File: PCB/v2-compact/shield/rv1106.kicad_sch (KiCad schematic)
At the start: 0 parts

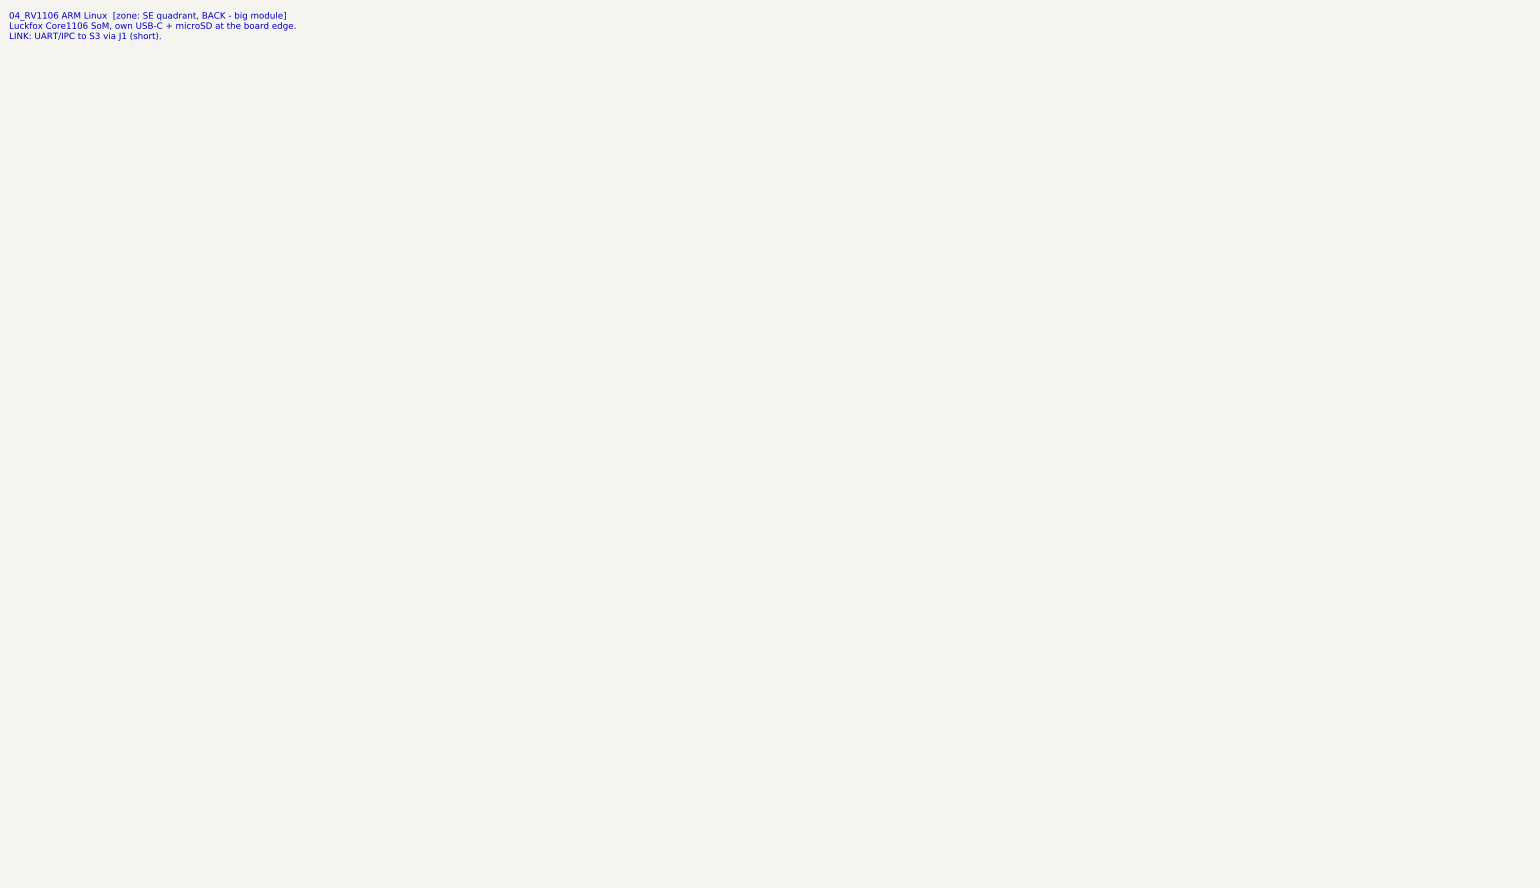
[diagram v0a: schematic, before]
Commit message: Schematics: HTRC110 and RV1106 sheets — full sheet set complete
- 08_LF_RFID_HTRC110: 5V HITAG reader, 3-wire (SCLK/DIN/DOUT) to the C5, DOUT
  open-drain pulled to 3.3V, 4MHz crystal, decoupling. LF coil tank flagged;
  pins 8-14 flagged to verify against the datasheet.
- 04_RV1106_Linux (A3): Core1106 SoM self-powered from its own USB-C (CC
  resistors) with its own microSD; UART to the S3 over J1 (RV_TX/RX/CTRL).
  Symbol is functional with placeholder pin numbers, flagged to verify against
  the Luckfox pinout.
- Add HTRC110 + RV1106 custom symbols to SnowOwl.kicad_sym.

All 17 sheets across both boards are now captured and netlist-verified
(153 nets). Remaining: ERC cleanup (no-connects + power flags), the two flagged
pinouts, RF matching values, and finishing the module footprints.
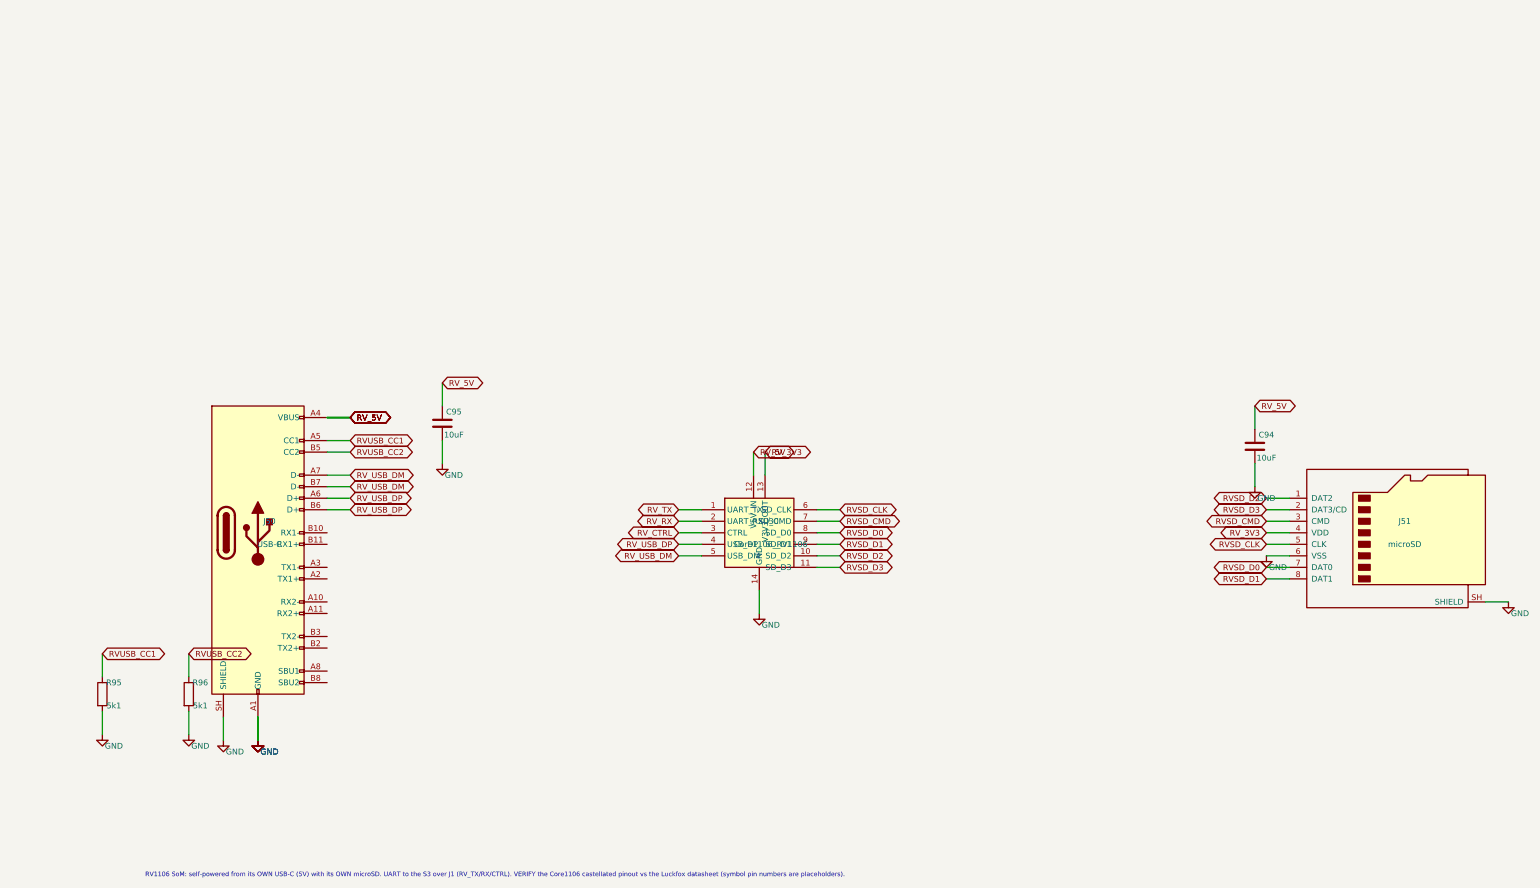
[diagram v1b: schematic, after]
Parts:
- added C94, C95: 10uF, Capacitor_SMD:C_0402_1005Metric, symbol Device:C
- added J50: USB-C, Connector_USB:USB_C_Receptacle_HRO_TYPE-C-31-M-12, symbol Connector:USB_C_Receptacle
- added J51: microSD, Connector_Card:microSD_HC_Hirose_DM3AT-SF-PEJM5, symbol Connector:Micro_SD_Card
- added R95, R96: 5k1, Resistor_SMD:R_0402_1005Metric, symbol Device:R
- added U30: Core1106_RV1106, symbol SnowOwl:RV1106_Core1106
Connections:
- new net GND: C94.2, C95.2, J50.A1 (GND), J50.A12 (GND), J50.B1 (GND), J50.B12 (GND), J50.SH (SHIELD), J51.6 (VSS), J51.SH (SHIELD), R95.2, R96.2, U30.14 (GND)
- new net RVSD_CLK: J51.5 (CLK), U30.6 (SD_CLK)
- new net RVSD_CMD: J51.3 (CMD), U30.7 (SD_CMD)
- new net RVSD_D0: J51.7 (DAT0), U30.8 (SD_D0)
- new net RVSD_D1: J51.8 (DAT1), U30.9 (SD_D1)
- new net RVSD_D2: J51.1 (DAT2), U30.10 (SD_D2)
- new net RVSD_D3: J51.2 (DAT3/CD), U30.11 (SD_D3)
- new net RVUSB_CC1: J50.A5 (CC1), R95.1
- new net RVUSB_CC2: J50.B5 (CC2), R96.1
- new net RV_3V3: J51.4 (VDD), U30.13 (V3V3_OUT)
- new net RV_5V: C94.1, C95.1, J50.A4 (VBUS), J50.A9 (VBUS), J50.B4 (VBUS), J50.B9 (VBUS), U30.12 (V5V_IN)
- new net RV_CTRL: U30.3 (CTRL)
- new net RV_RX: U30.2 (UART_RX)
- new net RV_TX: U30.1 (UART_TX)
- new net RV_USB_DM: J50.A7 (D-), J50.B7 (D-), U30.5 (USB_DM)
- new net RV_USB_DP: J50.A6 (D+), J50.B6 (D+), U30.4 (USB_DP)
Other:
- note added: "RV1106 SoM: self-powered from its OWN USB-C (5V) with its OWN microSD. UART to the S3 over J1 (RV_TX/RX/CTRL). VERIFY the Core1106 castellated pinout vs the Luckfox datasheet (symbol pin numbers are placeholders)."
- note removed: "04_RV1106 ARM Linux [zone: SE quadrant, BACK - big module] Luckfox Core1106 SoM, own USB-C + microSD at the board edge. LINK: UART/IPC to S3 via J1 (short)."

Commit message: Schematic: set U30 (RV1106) footprint (generator wrote it empty for the custom SnowOwl symbol)
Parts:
- U30: footprint (none) -> SnowOwl:RV1106_Core1106
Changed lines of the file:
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@@
     (property "Reference" "U30" (at 182.88 127 0) (effects (font (size 1.27 1.27))))
     (property "Value" "Core1106_RV1106" (at 182.88 132.08 0) (effects (font (size 1.27 1.27))))
-    (property "Footprint" "" (at 180.34 129.54 0) (effects (font (size 1.27 1.27)) hide))
+    (property "Footprint" "SnowOwl:RV1106_Core1106" (at 180.34 129.54 0) (effects (font (size 1.27 1.27)) hide))
     (pin "1")
     (pin "2")

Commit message: Schematic: add battery + USB-C charger power subsystem (BQ25896, 2500mAh)
Adds the full power section to the shield's power sheet, per the battery/stacking research:
- USB-C (J50 VBUS) -> BQ25896 (3A switch-mode charger + power-path + I2C). Charges a 2500mAh
  1S LiPo (BT50, JST-PH) through DW01A/FS8205 protection (U56); MAX17048 fuel gauge (U57).
- Power-path SYS -> TPS63020 buck-boost = system +3V3 (holds regulation as the cell sags),
  and -> TPS61230A boost = system +5V (feeds the RV1106). AP7361C LDO still makes clean C5_VDD.
- Rewired: J50 is now the charge/data input (VBUS), and the RV1106 is powered from the system
  +5V rail instead of being self-powered. +5V/+3V3 distribute to both boards over J1.
- New functional symbols (BQ25896/TPS63020/MAX17048/TPS61230A/DW01) in SnowOwl.kicad_sym.

Verified by KiCad's netlister: GND=79 (top net, intact), VBUS=3, VBAT=6, VSYS=8, +5V=13,
+3V3=36 - all rails distinct, no merges. Fixed two stub-collision shorts found while building
(input cap on the charger's pin column; VBAT power-flag on a cap column) and upgraded
find_shorts.py to catch pin-on-wire collisions, not just endpoint snaps.

FIRST-PASS: IC pinouts + passive values are placeholders to VERIFY vs datasheets. The power
PARTS still need placing on the PCB (next step), and the main board's own USB/LDO reconciled.
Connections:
- net RV_5V renamed VBUS
- net VBUS: no longer C94.1, C95.1, U30.12 (V5V_IN)
- new net +5V: C94.1, C95.1, U30.12 (V5V_IN)
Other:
- note added: "RV1106 SoM: powered from the system +5V rail (battery boost). J50 USB-C brings in VBUS (charge input) + its own USB data + microSD. UART to the S3 over J1 (RV_TX/RX/CTRL). VERIFY the Core1106 castellated pinout vs the Luckfox datasheet (symbol pin numbers are placeholders)."
- note removed: "RV1106 SoM: self-powered from its OWN USB-C (5V) with its OWN microSD. UART to the S3 over J1 (RV_TX/RX/CTRL). VERIFY the Core1106 castellated pinout vs the Luckfox datasheet (symbol pin numbers are placeholders)."

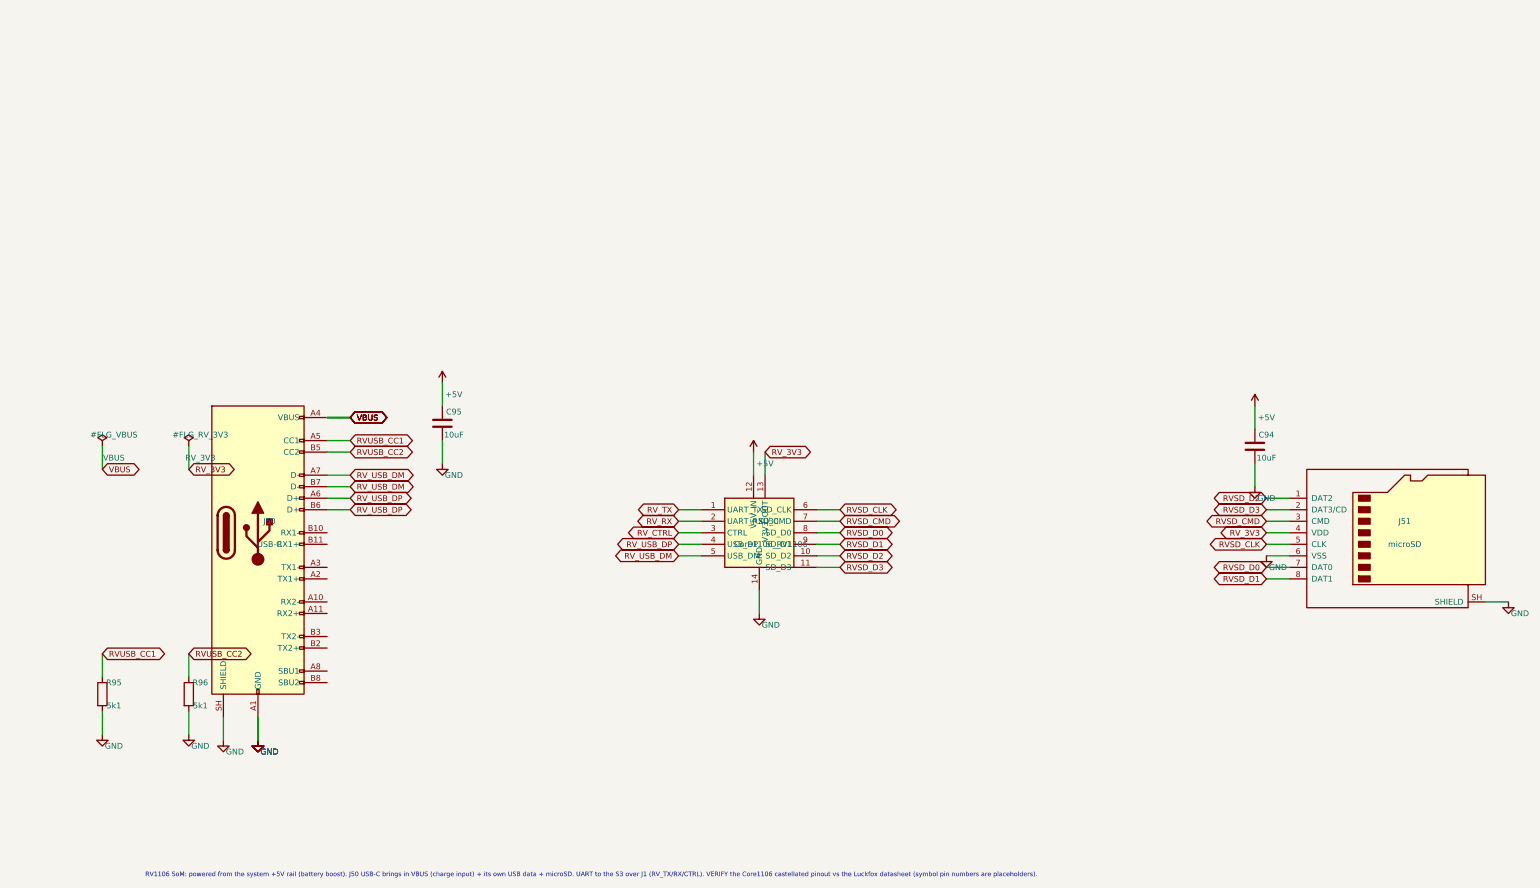
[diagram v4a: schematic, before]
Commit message: Single USB-C + battery power; J1 vertical on the left edge; U30 model; back-side comments
Power/architecture:
- Remove J50 (the RV1106's own USB-C). The device now has ONE USB-C: the main board's J20.
  J20's VBUS is carried over J1 pin19 (was SPARE) to the shield's BQ25896 charger, so charging +
  the ESP32-S3 data/programming share the single port. Everything runs off the battery.
- Reconcile the nets: J20 VBUS -> VBUS (was VBUS_MAIN), charger VBUS <- J1 pin19, RV1106 keeps its
  microSD (J51) but loses its USB port (reached over UART on J1). Removed orphans R95/R96 (J50 CC
  resistors) and the redundant main LDO U21. Verified: J1 mates 20/20 on both boards, VBUS spans
  J20 -> J1 -> U55, GND healthy (106/37 nodes), no bad net merges.

Placement:
- J1 stack header: was horizontal mid-board, now VERTICAL on the WEST edge at the same spot on both
  boards (they still mate). Nudged the shield's PN532/flash/HTRC (U7/U12/U8) east to clear it, and
  the main's screen east. Status LEDs D10/D11 pulled off the corner mounting holes. 0 real overlaps.

3D + silk:
- U30 (RV1106 Core1106): no KiCad model exists for the Luckfox SoM -> add a sized VRML module
  stand-in (SnowOwl.3dshapes/RV1106_Core1106.wrl; sizes pre-divided by 2.54 for KiCad's inch-unit
  VRML reader). USB-C model: swap the vertical USB4085 for the 16-pin horizontal USB4105 so it
  seats correctly against the horizontal HRO footprint.
- ESP32-BlackRaven art: logo moved to the top by the LEDs, raven dropped down to fill the board.
  Dropped the cluttering TFT label (fab outline kept). Added five back-side silkscreen comments on
  the main board (title/rev, battery, power path, USB-C role, J1 purpose).

Deferred (SWIG pcbnew geometry calls are failing in this environment right now): re-pour the inner
GND/+3V3 planes (inner layers, not visible in renders); apply the datasheet pinout/value fixes to
the power ICs (BQ25896/TPS63020/TPS61230A/MAX17048).
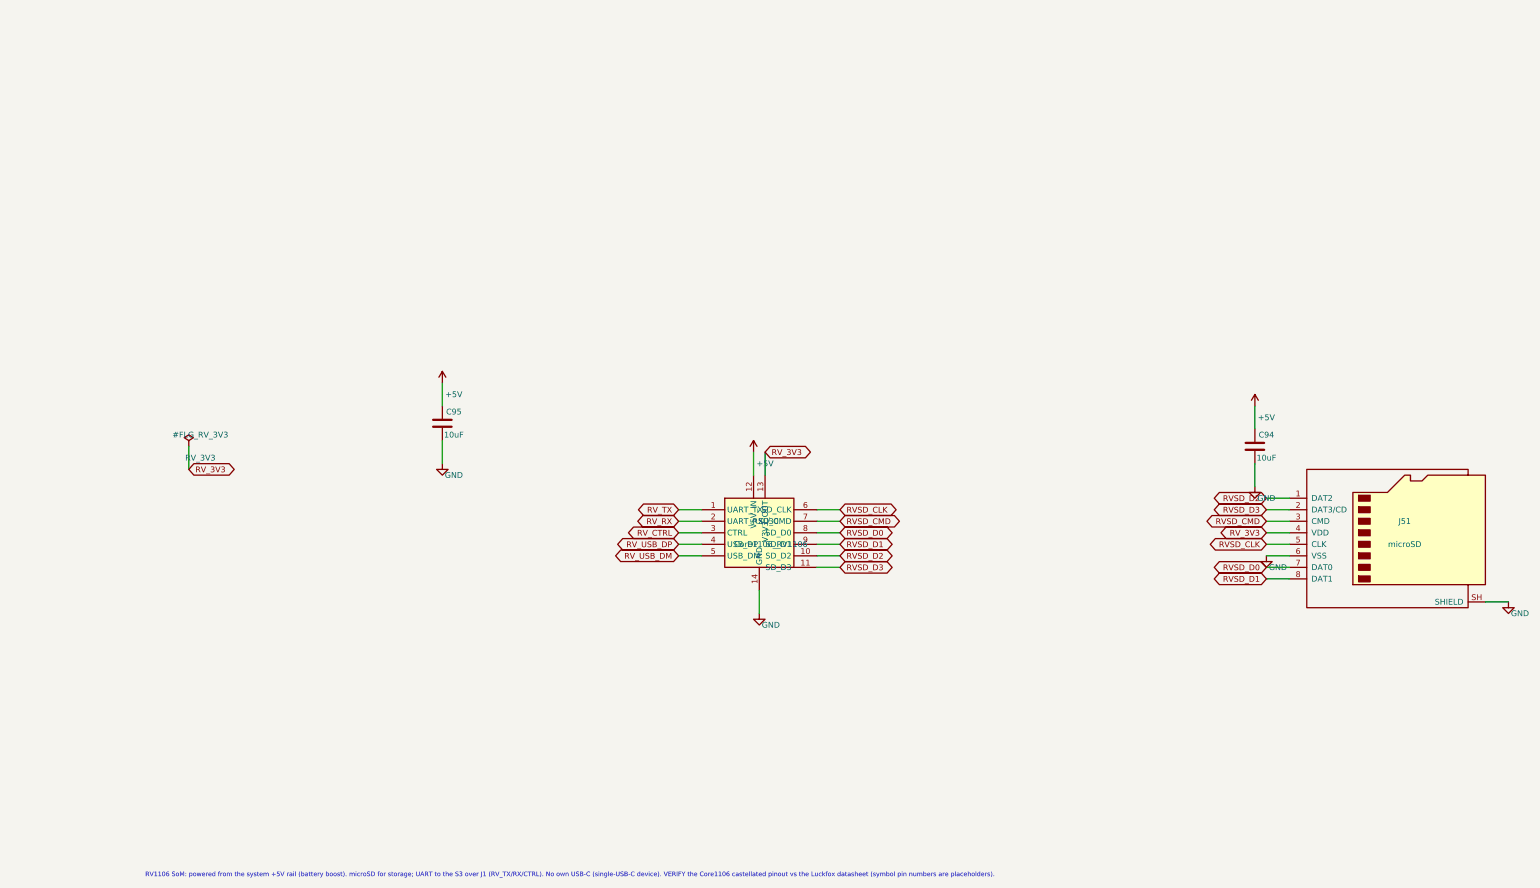
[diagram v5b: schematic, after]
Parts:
- removed J50: USB-C, Connector_USB:USB_C_Receptacle_HRO_TYPE-C-31-M-12, symbol Connector:USB_C_Receptacle
- removed R95, R96: 5k1, Resistor_SMD:R_0402_1005Metric, symbol Device:R
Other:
- note added: "RV1106 SoM: powered from the system +5V rail (battery boost). microSD for storage; UART to the S3 over J1 (RV_TX/RX/CTRL). No own USB-C (single-USB-C device). VERIFY the Core1106 castellated pinout vs the Luckfox datasheet (symbol pin numbers are placeholders)."
- note removed: "RV1106 SoM: powered from the system +5V rail (battery boost). J50 USB-C brings in VBUS (charge input) + its own USB data + microSD. UART to the S3 over J1 (RV_TX/RX/CTRL). VERIFY the Core1106 castellated pinout vs the Luckfox datasheet (symbol pin numbers are placeholders)."
